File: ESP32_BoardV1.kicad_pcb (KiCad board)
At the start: 2 copper layers, 95 x 55 mm, 31 parts, among them J1 Jack-DC, J2 MODBUS RTU, J3 ISP, J4 EXT. IO 1, J5 To Sensor, J6 EXT. IO 1, Q1 UMH3N, U1 MAX485E, U2 ESP32-WROOM-32E(8MB), U3 RT9078-33GJ5

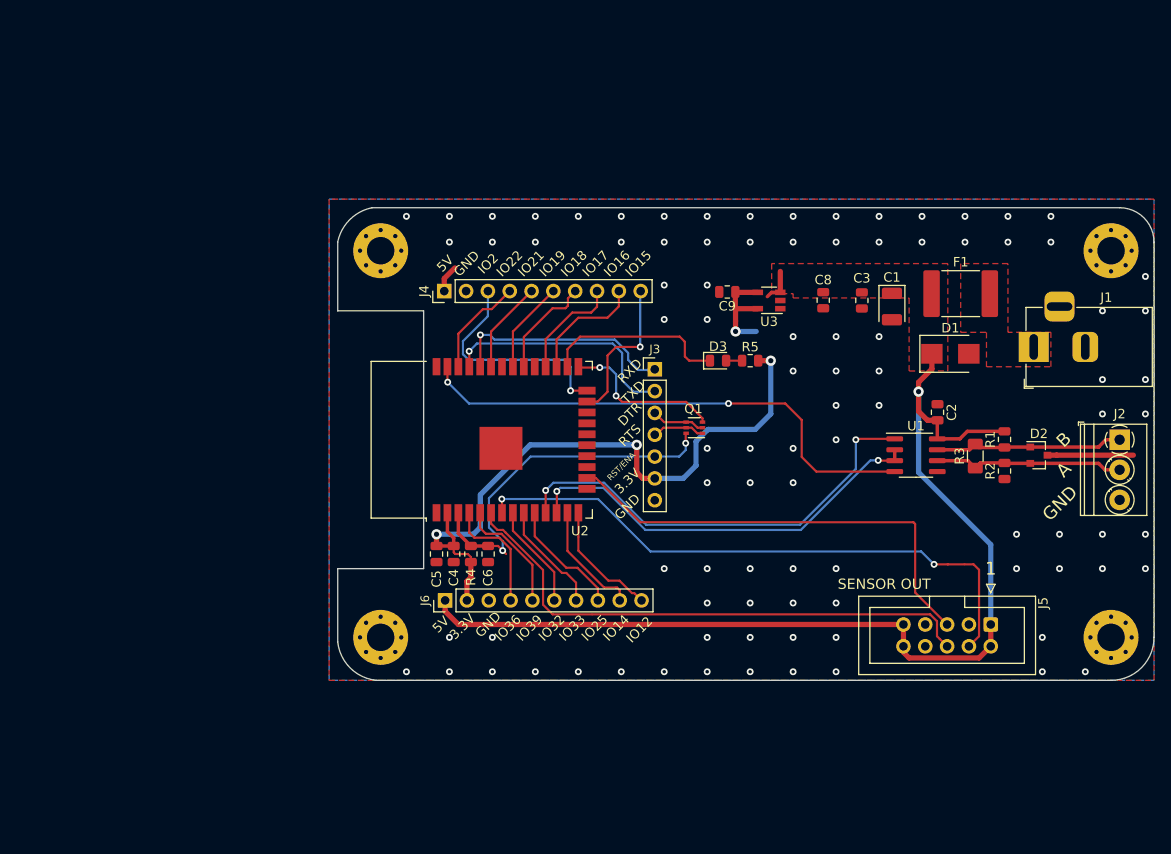
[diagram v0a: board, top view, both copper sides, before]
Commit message: Recreated PCB file
Removed old PCB files, Schematic error in existing PCB has been rectfied
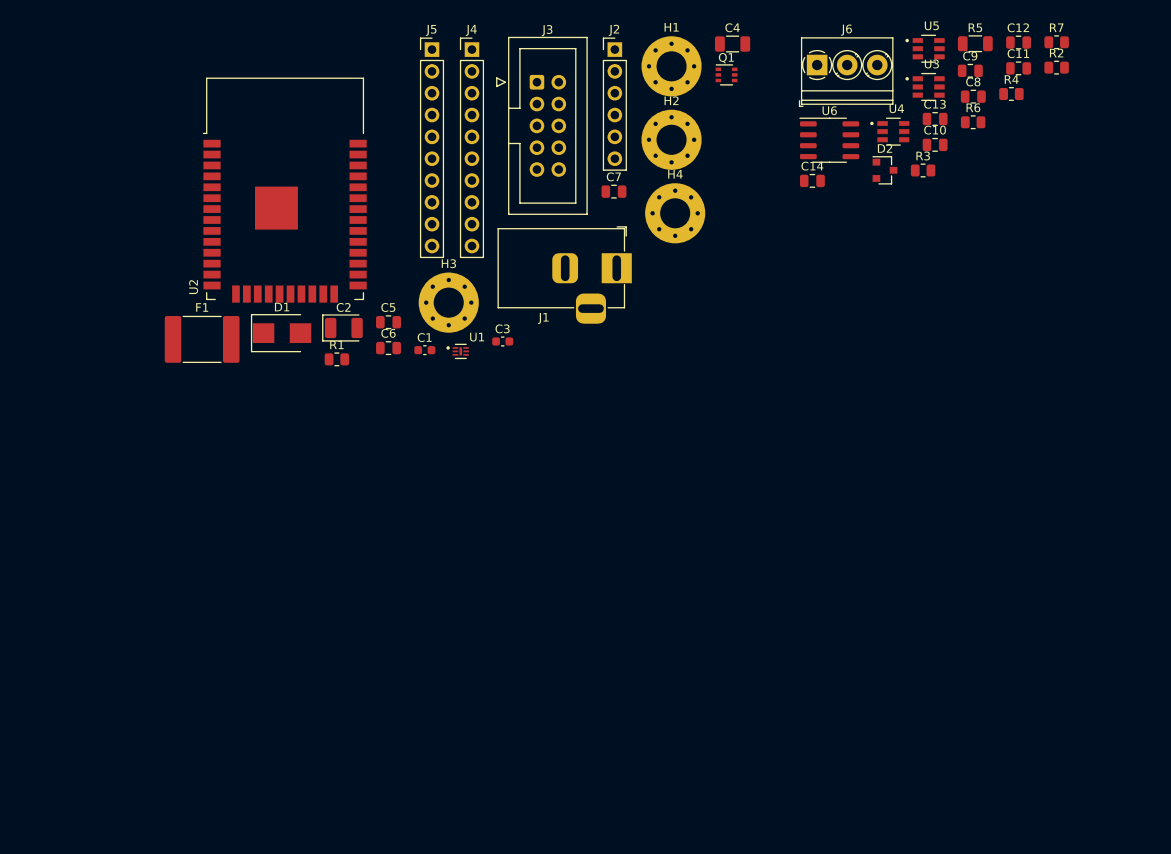
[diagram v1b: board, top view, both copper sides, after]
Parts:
- removed D3: LED, LED_SMD:LED_0805_2012Metric
- added C10: 10uF, Capacitor_SMD:C_0805_2012Metric, F.Cu at (191.5, 77.7)
- added C11: 10uF, Capacitor_SMD:C_0805_2012Metric, F.Cu at (201.2, 68.8)
- added C12: 10uF, Capacitor_SMD:C_0805_2012Metric, F.Cu at (201.2, 65.8)
- added C13: 10uF, Capacitor_SMD:C_0805_2012Metric, F.Cu at (191.5, 74.7)
- added C14: 0.1uF, Capacitor_SMD:C_0805_2012Metric, F.Cu at (177.2, 81.9)
- added C7: 0.1uF, Capacitor_SMD:C_0805_2012Metric, F.Cu at (154.2, 83.1)
- added R6: 10k, Resistor_SMD:R_0805_2012Metric, F.Cu at (196.0, 75.1)
- added R7: 10k, Resistor_SMD:R_0805_2012Metric, F.Cu at (205.7, 65.7)
- added U4: TXB0101DBVR, SnapEDA Library:SOT95P280X145-6N, F.Cu at (186.7, 76.1)
- added U5: TXB0101DBVR, SnapEDA Library:SOT95P280X145-6N, F.Cu at (190.8, 66.5)
- added U6: MAX485E, Package_SO:SOIC-8_3.9x4.9mm_P1.27mm, F.Cu at (179.2, 77.1)
- C1: value 100uF -> 2.2uF; footprint Capacitor_Tantalum_SMD:CP_EIA-3528-21_Kemet-B -> Capacitor_SMD:C_0603_1608Metric
- C2: value 0.1uF -> 100uF; footprint Capacitor_SMD:C_0805_2012Metric -> Capacitor_Tantalum_SMD:CP_EIA-3528-21_Kemet-B
- C3: value 0.1uF -> 2.2uF; footprint Capacitor_SMD:C_0805_2012Metric -> Capacitor_SMD:C_0603_1608Metric
- C4: value 10uF -> 100uF; footprint Capacitor_SMD:C_0805_2012Metric -> Capacitor_SMD:C_1206_3216Metric
- C5: value 0.1uF -> 10uF
- C8, C9: value 2.2uF -> 10uF
- H1, H2, H3, H4: value MountingHole -> MountingHole_Pad; footprint MountingHole:MountingHole_3.2mm_M3_Pad_Via -> MountingHole:MountingHole_3.5mm_Pad_Via
- J1: value Jack-DC -> Barrel_Jack_Switch
- J2: value MODBUS RTU -> ISP; footprint TerminalBlock_Phoenix:TerminalBlock_Phoenix_PT-1,5-3-3.5-H_1x03_P3.50mm_Horizontal -> Connector_PinHeader_2.54mm:PinHeader_1x06_P2.54mm_Vertical
- J3: value ISP -> To Sensor; footprint Connector_PinHeader_2.54mm:PinHeader_1x07_P2.54mm_Vertical -> Connector_IDC:IDC-Header_2x05_P2.54mm_Vertical
- J5: value To Sensor -> EXT. IO 1; footprint Connector_IDC:IDC-Header_2x05_P2.54mm_Vertical -> Connector_PinHeader_2.54mm:PinHeader_1x10_P2.54mm_Vertical
- J6: value EXT. IO 1 -> MODBUS RTU; footprint Connector_PinHeader_2.54mm:PinHeader_1x10_P2.54mm_Vertical -> TerminalBlock_Phoenix:TerminalBlock_Phoenix_PT-1,5-3-3.5-H_1x03_P3.50mm_Horizontal
- R1: value 4K7 -> 10K
- R2: value 4K7 -> 10k
- R3: value 120R -> 10k; footprint Resistor_SMD:R_1206_3216Metric -> Resistor_SMD:R_0805_2012Metric
- R4: value 10K -> 10k
- R5: value 1K -> 120R; footprint Resistor_SMD:R_0805_2012Metric -> Resistor_SMD:R_1206_3216Metric
- U1: value MAX485E -> MIC5528-3.3YMT-TR; footprint Package_SO:SOIC-8_3.9x4.9mm_P1.27mm -> SnapEDA Library:SON40P120X120X60-7N
- U3: value RT9078-33GJ5 -> TXB0101DBVR; footprint Package_TO_SOT_SMD:TSOT-23-5 -> SnapEDA Library:SOT95P280X145-6N
- moved J5 93.3 mm to (133.0, 66.6), turned to 0 degrees
- moved F1 88.4 mm to (106.2, 100.3)
- moved R4 82.6 mm to (200.4, 71.8), turned to 0 degrees
- moved R1 78.3 mm to (121.9, 102.6), turned to 0 degrees
- moved D1 77.8 mm to (115.5, 99.6)
- moved J6 75.9 mm to (177.8, 68.4), turned to 0 degrees
- moved J2 74.2 mm to (154.3, 66.6), turned to 0 degrees
- moved H4 70.8 mm to (161.3, 85.6)
- moved C2 69.8 mm to (122.7, 99.0), turned to 0 degrees
- moved C4 67.6 mm to (168.0, 65.9), turned to 0 degrees
- moved C1 54.6 mm to (132.1, 101.6), turned to 0 degrees
- moved U1 54.3 mm to (136.3, 101.7)
- moved H2 52.7 mm to (160.9, 77.1)
- moved J1 49.4 mm to (154.5, 92.0), turned to 0 degrees
- moved R2 47.3 mm to (205.7, 68.7), turned to 0 degrees
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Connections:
- C1 pad 2: GND -> +5V
- C2 pad 1: GND -> +5V
- C3 pad 1: +5V -> +3V3
- C3 pad 2: GND -> +5V
- C4 pad 1: +3V3 -> /RESET
- C4 pad 2: GND -> +5V
- C5 pad 2: GND -> +5V
- C6 pad 2: GND -> +5V
- C8 pad 1: +5V -> +3V3
- C8 pad 2: GND -> +5V
- C9 pad 2: GND -> +5V
- D1 pad 2: GND -> +5V
- D2 pad 1: /B -> /Modubus/B
- D2 pad 2: /A -> /Modubus/A
- D2 pad 3: GND -> +5V
- H1 pad 1: (no net) -> +5V
- H2 pad 1: (no net) -> +5V
- H3 pad 1: (no net) -> +5V
- H4 pad 1: (no net) -> +5V
- J1 pad 2: GND -> +5V
- J1 pad 3: (no net) -> +5V
- J2 pad 1: /B -> /UART0_RXD
- J2 pad 2: /A -> /UART0_TXD
- J2 pad 3: GND -> /DTR
- J3 pad 1: /UART0_RXD -> +5V
- J3 pad 2: /UART0_TXD -> +5V
- J3 pad 3: /DTR -> +5V
- J3 pad 4: /RTS -> /GAS_AOUT
- J3 pad 5: /RESET -> /SHARP_ILED
- J3 pad 6: +3V3 -> /SHARP_AOUT
- J3 pad 7: GND -> Net-(J3-Pad7)
- J4 pad 2: GND -> +5V
- J5 pad 10: +5V -> /IO12
- J5 pad 2: +5V -> +3V3
- J5 pad 3: GND -> +5V
- J5 pad 4: /GAS_AOUT -> /IO36
- J5 pad 5: /SHARP_ILED -> /IO39
- J5 pad 6: /SHARP_AOUT -> /IO32
- J5 pad 7: (no net) -> /IO33
- J5 pad 8: GND -> /IO25
- J5 pad 9: +5V -> /IO14
- J6 pad 1: +5V -> /Modubus/B
- J6 pad 2: +3V3 -> /Modubus/A
- J6 pad 3: GND -> +5V
- R1 pad 1: /B -> +3V3
- R1 pad 2: +5V -> /RESET
- R2 pad 1: GND -> +5V
- R2 pad 2: /A -> /Modubus/MODBUS_TXD5V
- R3 pad 1: /A -> +5V
- R3 pad 2: /B -> /Modubus/MODBUS_RXD5V
- R4 pad 1: +3V3 -> +5V
- R4 pad 2: /RESET -> /Modubus/MODBUS_EN5V
- R5 pad 1: +3V3 -> /Modubus/A
- R5 pad 2: Net-(D3-Pad2) -> /Modubus/B
- U1 pad 1: /MODBUS_RXD -> +3V3
- U1 pad 2: /MODBUS_EN -> +3V3
- U1 pad 3: /MODBUS_EN -> +5V
- U1 pad 4: /MODBUS_TXD -> +5V
- U1 pad 5: GND -> (no net)
- U1 pad 6: /A -> +5V
- U1 pad 7: /B -> +5V
- U2 pad 1: GND -> +5V
- U2 pad 15: GND -> +5V
- U2 pad 17: (no net) -> Net-(U2-Pad17)
- U2 pad 18: (no net) -> Net-(U2-Pad18)
- U2 pad 19: (no net) -> Net-(U2-Pad19)
- U2 pad 20: (no net) -> Net-(U2-Pad20)
- U2 pad 21: (no net) -> Net-(U2-Pad21)
- U2 pad 22: (no net) -> Net-(U2-Pad22)
- U2 pad 26: Net-(D3-Pad1) -> /IO4
- U2 pad 29: (no net) -> /IO5
- U2 pad 32: (no net) -> Net-(U2-Pad32)
- U2 pad 38: GND -> +5V
- U2 pad 39: GND -> +5V
- U3 pad 1: +5V -> +3V3
- U3 pad 2: GND -> +5V
- U3 pad 3: +5V -> /Modubus/MODBUS_EN
- U3 pad 4: +3V3 -> /Modubus/MODBUS_EN5V
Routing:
- net +5V: track 130.5 -> 0.00 mm, vias 1 -> 0
- net +3V3: track 89.1 -> 0.00 mm, vias 4 -> 0
- net /GAS_AOUT: track 70.0 -> 0.00 mm, vias 2 -> 0
- net /SHARP_AOUT: track 63.6 -> 0.00 mm
- net /MODBUS_TXD: track 60.7 -> 0.00 mm, vias 2 -> 0
- net /SHARP_ILED: track 53.6 -> 0.00 mm
- net /MODBUS_RXD: track 51.8 -> 0.00 mm, vias 2 -> 0
- net /MODBUS_EN: track 48.7 -> 0.00 mm, vias 2 -> 0
- net /RESET: track 42.9 -> 0.00 mm, vias 2 -> 0
- net /UART0_TXD: track 28.1 -> 0.00 mm, vias 1 -> 0
- net /IO2: track 26.4 -> 0.00 mm, vias 1 -> 0
- net /UART0_RXD: track 26.3 -> 0.00 mm, vias 1 -> 0
- net /A: track 22.9 -> 0.00 mm
- net /B: track 22.5 -> 0.00 mm
- net Net-(D3-Pad1): track 21.4 -> 0.00 mm
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- removed copper zone on F.Cu, net +5V
- removed copper zone on B.Cu, net GND
- removed copper zone on F.Cu, net GND
- removed copper zone on F.Cu, net Net-(F1-Pad2)
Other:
- board outline removed
- board text removed: "1"
- board text removed: "3.3V"
- board text removed: "5V"
- board text removed: "A"
- board text removed: "B"
- board text removed: "DTR"
- board text removed: "GND"
- board text removed: "IO12"
- board text removed: "IO14"
- board text removed: "IO15"
- board text removed: "IO16"
- board text removed: "IO17"
- board text removed: "IO18"
- board text removed: "IO19"
- board text removed: "IO2"
- board text removed: "IO21"
- board text removed: "IO22"
- board text removed: "IO25"
- board text removed: "IO32"
- board text removed: "IO33"
- board text removed: "IO36"
- board text removed: "IO39"
- board text removed: "RST/ENA"
- board text removed: "RTS"
- board text removed: "RXD"
- board text removed: "SENSOR OUT"
- board text removed: "TXD"

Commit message: 24.12.21
Board layout added, Step file added
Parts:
- removed C11, C12, C13: 10uF, Capacitor_SMD:C_0805_2012Metric
- removed the C4 at (168.0, 65.9)
- removed the C8 at (196.0, 72.1)
- removed the R6 at (196.0, 75.1)
- removed U4, U5: TXB0101DBVR, SnapEDA Library:SOT95P280X145-6N
- removed U6: MAX485E, Package_SO:SOIC-8_3.9x4.9mm_P1.27mm
- added C7: 0.1uF, Capacitor_SMD:C_0402_1005Metric_Pad0.74x0.62mm_HandSolder, F.Cu at (105.0, 105.0)
- added J7: Display, Connector_FFC-FPC:Hirose_FH12-40S-0.5SH_1x40-1MP_P0.50mm_Horizontal, F.Cu at (180.0, 125.0)
- added JP1: SolderJumper_2_Open, Resistor_SMD:R_0402_1005Metric_Pad0.72x0.64mm_HandSolder, F.Cu at (116.5, 103.5)
- added JP2: SolderJumper_2_Open, Resistor_SMD:R_0402_1005Metric_Pad0.72x0.64mm_HandSolder, F.Cu at (116.5, 105.0)
- added R10: 10k, Resistor_SMD:R_0402_1005Metric_Pad0.72x0.64mm_HandSolder, F.Cu at (174.0, 116.5)
- added R2: 10k, Resistor_SMD:R_0402_1005Metric_Pad0.72x0.64mm_HandSolder, F.Cu at (105.0, 103.5)
- added R7: 10k, Resistor_SMD:R_0805_2012Metric, F.Cu at (134.0, 105.8)
- added R9: 10k, Resistor_SMD:R_0402_1005Metric_Pad0.72x0.64mm_HandSolder, F.Cu at (174.0, 114.0)
- added SW1: SW_SPDT, Button_Switch_THT:SW_Slide_1P2T_CK_OS102011MS2Q, F.Cu at (102.8, 98.0)
- C1: value 2.2uF -> 10uF; footprint Capacitor_SMD:C_0603_1608Metric -> Capacitor_SMD:CP_Elec_3x5.4
- C10: value 10uF -> 0.1uF; footprint Capacitor_SMD:C_0805_2012Metric -> Capacitor_SMD:C_0402_1005Metric_Pad0.74x0.62mm_HandSolder
- C3: value 2.2uF -> 22uF; footprint Capacitor_SMD:C_0603_1608Metric -> Capacitor_SMD:CP_Elec_5x5.4
- C9: footprint Capacitor_SMD:C_0805_2012Metric -> Capacitor_SMD:C_0402_1005Metric_Pad0.74x0.62mm_HandSolder
- J1: footprint Connector_BarrelJack:BarrelJack_Horizontal -> Connector_BarrelJack:BarrelJack_CLIFF_FC681465S_SMT_Horizontal
- J3: value To Sensor -> GPIO expanded; footprint Connector_IDC:IDC-Header_2x05_P2.54mm_Vertical -> SnapEDA Library:JST_SM04B-SRSS-TB(LF)(SN)
- J4: value EXT. IO 1 -> sensor; footprint Connector_PinHeader_2.54mm:PinHeader_1x10_P2.54mm_Vertical -> connector:JST_SM05B-SRSS-TB(LF)(SN)
- J5: value EXT. IO 1 -> I2C extended; footprint Connector_PinHeader_2.54mm:PinHeader_1x10_P2.54mm_Vertical -> SnapEDA Library:JST_SM04B-SRSS-TB(LF)(SN)
- J6: footprint TerminalBlock_Phoenix:TerminalBlock_Phoenix_PT-1,5-3-3.5-H_1x03_P3.50mm_Horizontal -> SnapEDA Library:JST_SM03B-SRSS-TB(LF)(SN)
- R3: renamed from R2; value 10k -> 10K
- R4: renamed from R3; value 10k -> 10K
- R5: renamed from R4; value 10k -> 10K
- U1: value MIC5528-3.3YMT-TR -> AZ1117-3.3; footprint SnapEDA Library:SON40P120X120X60-7N -> Package_TO_SOT_SMD:SOT-223-3_TabPin2
- U3: value TXB0101DBVR -> MAX3485; footprint SnapEDA Library:SOT95P280X145-6N -> Package_SO:SOIC-8_3.9x4.9mm_P1.27mm
- moved H2 103.1 mm to (89.0, 151.0)
- moved R3 89.0 mm to (133.2, 120.5), turned to 90 degrees
- moved H3 85.9 mm to (201.0, 151.0)
- moved R5 84.6 mm to (131.2, 120.5), turned to 90 degrees
- moved C6 81.5 mm to (93.0, 137.0), turned to 180 degrees
- moved H1 78.0 mm to (89.0, 99.0)
- moved R8 75.2 mm to (142.0, 105.8)
- moved Q1 73.4 mm to (121.0, 126.5), turned to 180 degrees
- moved R6 70.5 mm to (138.0, 105.8)
- moved C9 70.1 mm to (176.5, 136.5), turned to 270 degrees
- moved U3 70.0 mm to (138.5, 117.5)
- moved R4 66.2 mm to (133.2, 114.5), turned to 270 degrees
- moved J2 66.0 mm to (114.0, 118.9)
- moved C10 61.1 mm to (175.0, 136.5), turned to 270 degrees
- moved J1 59.5 mm to (141.0, 150.0), turned to 90 degrees
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- renumbered C5 to C4, C6 to C5, C7 to C6, C14 to C8, R5 to R6, R7 to R8
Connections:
- C1 pad 2: +5V -> GND
- C10 pad 2: +5V -> GND
- C2 pad 2: +5V -> GND
- C3 pad 2: +5V -> GND
- C4 pad 2: +5V -> GND
- C5 pad 2: +5V -> GND
- C6 pad 2: +5V -> GND
- C8 pad 1: +5V -> GND
- C8 pad 2: +5V -> +3V3
- C9 pad 2: +5V -> GND
- D1 pad 2: +5V -> GND
- D2 pad 3: +5V -> GND
- H1 pad 1: +5V -> GND
- H2 pad 1: +5V -> GND
- H3 pad 1: +5V -> GND
- H4 pad 1: +5V -> GND
- J1 pad 2: +5V -> GND
- J1 pad 3: +5V -> GND
- J2 pad 6: +5V -> GND
- J3 pad 1: +5V -> /GPIO15
- J3 pad 2: +5V -> /GPIO16
- J3 pad 3: +5V -> /GPIO33
- J3 pad 4: /GAS_AOUT -> /GPIO32
- J4 pad 2: +5V -> /GAS_AOUT
- J4 pad 3: /IO2 -> /SHARP_AOUT
- J4 pad 4: /IO22 -> /SHARP_ILED
- J4 pad 5: /IO21 -> GND
- J5 pad 1: +5V -> /VCC
- J5 pad 2: +3V3 -> CTP_SCL
- J5 pad 3: +5V -> CTP_SDA
- J5 pad 4: /IO36 -> GND
- J6 pad 3: +5V -> GND
- R3 pad 1: +5V -> +3V3
- R3 pad 2: /Modubus/MODBUS_TXD5V -> /Modubus/MODBUS_TXD
- R4 pad 1: +5V -> +3V3
- R4 pad 2: /Modubus/MODBUS_RXD5V -> /Modubus/MODBUS_RXD
- R5 pad 1: +5V -> +3V3
- R5 pad 2: /Modubus/MODBUS_EN5V -> /Modubus/MODBUS_EN
- R8 pad 2: +5V -> +3V3
- U1 pad 1: +3V3 -> GND
- U2 pad 1: +5V -> GND
- U2 pad 10: /IO25 -> CTP_INT
- U2 pad 13: /IO14 -> TFT_RST
- U2 pad 14: /IO12 -> Net-(U2-Pad14)
- U2 pad 15: +5V -> GND
- U2 pad 23: /IO15 -> /GPIO15
- U2 pad 24: /IO2 -> Net-(U2-Pad24)
- U2 pad 26: /IO4 -> TFT_AO
- U2 pad 27: /IO16 -> Net-(SW1-Pad2)
- U2 pad 28: /IO17 -> /GPIO17
- U2 pad 29: /IO5 -> TFT_CS
- U2 pad 30: /IO18 -> TFT_SCLK
- U2 pad 31: /IO19 -> TFT_SDI
- U2 pad 33: /IO21 -> CTP_SDA
- U2 pad 36: /IO22 -> CTP_SCL
- U2 pad 38: +5V -> GND
- U2 pad 39: +5V -> GND
- U2 pad 8: /IO32 -> /GPIO32
- U2 pad 9: /IO33 -> /GPIO33
- U3 pad 1: +3V3 -> /Modubus/MODBUS_RXD
- U3 pad 2: +5V -> /Modubus/MODBUS_EN
- U3 pad 4: /Modubus/MODBUS_EN5V -> /Modubus/MODBUS_TXD
- U3 pad 5: +3V3 -> GND
- U3 pad 6: +5V -> /Modubus/A
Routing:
- net /DTR: track 0.00 -> 8.99 mm
- net /RTS: track 0.00 -> 8.24 mm
- net /RESET: track 0.00 -> 6.85 mm
- net GND: vias 0 -> 37
- added copper zone on F.Cu, net +3V3
- added copper zone on F.Cu, net +5V
- added copper zone on B.Cu, net GND
- added copper zone on F.Cu, net Net-(F1-Pad2)
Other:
- board outline added: 120 x 60 mm
- board text added: "DTR"
- board text added: "GND"
- board text added: "RST"
- board text added: "RTS"
- board text added: "RXD"
- board text added: "TXD"

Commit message: PCB completed
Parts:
- moved J4 63.5 mm to (100.5, 153.0), turned to 0 degrees
- moved J5 49.6 mm to (124.4, 149.0), turned to 0 degrees
- moved J3 49.3 mm to (112.7, 149.0), turned to 0 degrees
- moved J6 48.5 mm to (135.6, 149.0), turned to 0 degrees
- moved JP1 43.8 mm to (122.0, 147.0), turned to 0 degrees
- moved JP2 40.9 mm to (122.0, 145.5), turned to 0 degrees
- moved R7 39.1 mm to (131.5, 144.8)
- moved R6 39.1 mm to (135.6, 144.8)
- moved R8 39.1 mm to (139.8, 144.8)
- moved C3 23.1 mm to (181.0, 148.8), turned to 90 degrees
- moved D1 15.3 mm to (165.0, 137.0), turned to 90 degrees
- moved D2 13.6 mm to (135.6, 128.2), turned to 270 degrees
- moved U1 12.6 mm to (173.5, 149.2)
- moved J1 12.0 mm to (153.0, 149.5)
- moved F1 12.0 mm to (153.0, 139.2)
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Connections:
- J3 pad 1: /GPIO15 -> /GPIO33
- J3 pad 2: /GPIO16 -> /GPIO17
- J3 pad 3: /GPIO33 -> /GPIO15
- J3 pad 4: /GPIO32 -> /GPIO16
- J4 pad 2: /GAS_AOUT -> /SHARP_AOUT
- J4 pad 3: /SHARP_AOUT -> /GAS_AOUT
- J6 pad 1: /Modubus/B -> /Modubus/A
- J6 pad 2: /Modubus/A -> GND
- J6 pad 3: GND -> /Modubus/B
- R3 pad 2: /Modubus/MODBUS_TXD -> MODBUS_TXD
- R4 pad 2: /Modubus/MODBUS_RXD -> MODBUS_RXD
- R5 pad 2: /Modubus/MODBUS_EN -> MODBUS_EN
- R7 pad 1: GND -> +3V3
- R8 pad 2: +3V3 -> GND
- U2 pad 10: CTP_INT -> /GPIO17
- U2 pad 11: /MODBUS_RXD -> MODBUS_RXD
- U2 pad 12: /MODBUS_EN -> MODBUS_EN
- U2 pad 16: /SHARP_ILED -> /GPIO16
- U2 pad 28: /GPIO17 -> CTP_INT
- U2 pad 37: /MODBUS_TXD -> MODBUS_TXD
- U2 pad 8: /GPIO32 -> /SHARP_ILED
- U3 pad 1: /Modubus/MODBUS_RXD -> MODBUS_RXD
- U3 pad 2: /Modubus/MODBUS_EN -> MODBUS_EN
- U3 pad 3: /Modubus/MODBUS_EN -> MODBUS_EN
- U3 pad 4: /Modubus/MODBUS_TXD -> MODBUS_TXD
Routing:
- net CTP_SDA: track 0.00 -> 139.1 mm, vias 0 -> 4
- net CTP_SCL: track 0.00 -> 138.3 mm, vias 0 -> 4
- net TFT_SDI: track 0.00 -> 93.3 mm
- net TFT_SCLK: track 0.00 -> 89.7 mm
- net +5V: track 0.00 -> 89.6 mm, vias 0 -> 1
- net TFT_CS: track 0.00 -> 86.5 mm
- net TFT_AO: track 0.00 -> 71.3 mm
- net TFT_RST: track 0.00 -> 70.9 mm, vias 0 -> 2
- net MODBUS_EN: track 0.00 -> 54.7 mm
- net MODBUS_RXD: track 0.00 -> 51.1 mm
- net MODBUS_TXD: track 0.00 -> 45.5 mm, vias 0 -> 2
- net +3V3: track 0.00 -> 41.7 mm, vias 0 -> 3
- net GND: track 0.00 -> 37.4 mm, vias 37 -> 56
- net /GPIO15: track 0.00 -> 34.4 mm, vias 0 -> 2
- net /RESET: track 6.85 -> 38.2 mm, vias 0 -> 1
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
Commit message: Schematics change
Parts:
- removed JP2: SolderJumper_2_Open, Resistor_SMD:R_0402_1005Metric_Pad0.72x0.64mm_HandSolder
- added REF**: WEEE-Logo_8.4x12mm_SilkScreen, Symbol:WEEE-Logo_8.4x12mm_SilkScreen, F.Cu at (167.5, 102.0)
- F1: footprint Fuse:Fuse_2920_7451Metric -> Fuse:Fuse_1206_3216Metric
- moved C7 6.75 mm to (111.8, 105.2)
- moved R2 6.75 mm to (111.8, 103.8)
- moved SW1 6.75 mm to (109.5, 97.8)
- moved JP1 2.83 mm to (120.0, 149.0), turned to 90 degrees
- moved F1 2.10 mm to (152.0, 141.0)
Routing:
- net CTP_INT: track 0.00 -> 86.3 mm
- net GND: track 37.4 -> 105.4 mm, vias 56 -> 72
- net +5V: track 89.6 -> 69.2 mm, vias 1 -> 3
- net TFT_SDI: track 93.3 -> 101.0 mm
- net TFT_SCLK: track 89.7 -> 96.2 mm
- net CTP_SCL: track 138.3 -> 144.5 mm
- net +3V3: track 41.7 -> 47.1 mm, vias 3 -> 2
- net TFT_CS: track 86.5 -> 91.4 mm
- net Net-(SW1-Pad2): track 22.4 -> 19.3 mm
- net CTP_SDA: track 139.1 -> 142.1 mm
- net /RESET: track 38.2 -> 40.9 mm
- net /UART0_RXD: track 18.7 -> 21.4 mm
- net MODBUS_TXD: track 45.5 -> 42.9 mm
- net /UART0_TXD: track 20.3 -> 22.4 mm
- net MODBUS_EN: track 54.7 -> 53.5 mm
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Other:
- outline, holes or cut-outs redrawn
- board text added: "A"
- board text added: "B"
- board text added: "GAS_AOUT"
- board text added: "GPI033"
- board text added: "GPIO15"
- board text added: "GPIO16"
- board text added: "GPIO17"
- board text added: "SCL"
- board text added: "SDA"
- board text added: "SEN_PWR"
- board text added: "SHARP_AOUT"
- board text added: "SHARP_ILED"
- board text added: "VCC"

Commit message: Final draft
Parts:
- removed JP1: SolderJumper_2_Open, Resistor_SMD:R_0402_1005Metric_Pad0.72x0.64mm_HandSolder
- removed REF**: WEEE-Logo_8.4x12mm_SilkScreen, Symbol:WEEE-Logo_8.4x12mm_SilkScreen
- added Q2: SS8050-G, Package_TO_SOT_SMD:SOT-23, F.Cu at (157.6, 133.4)
- added R11: 10K, Resistor_SMD:R_0402_1005Metric_Pad0.72x0.64mm_HandSolder, F.Cu at (154.8, 133.8)
- added R12: 10K, Resistor_SMD:R_0402_1005Metric_Pad0.72x0.64mm_HandSolder, F.Cu at (154.8, 134.8)
- added R13: 10R, Resistor_SMD:R_0402_1005Metric_Pad0.72x0.64mm_HandSolder, F.Cu at (171.2, 133.6)
- R7, R8: value 10k -> 5k
- moved R6 2.25 mm to (135.6, 142.5)
- moved R7 2.25 mm to (131.5, 142.5)
- moved R8 2.25 mm to (139.8, 142.5)
- moved C10 2.02 mm to (171.2, 134.6), turned to 180 degrees
- moved C7 1.85 mm to (111.8, 103.4)
- moved R2 1.35 mm to (111.8, 102.4)
- moved C9 1.20 mm to (171.2, 135.6), turned to 180 degrees
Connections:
- J3 pad 4: /GPIO16 -> +3V3
- J5 pad 1: /VCC -> +3V3
- J7 pad 2: GND -> /LED_K
- U2 pad 14: Net-(U2-Pad14) -> unconnected-(U2-Pad14)
- U2 pad 16: /GPIO16 -> /BL_CONTRL
- U2 pad 17: Net-(U2-Pad17) -> unconnected-(U2-Pad17)
- U2 pad 18: Net-(U2-Pad18) -> unconnected-(U2-Pad18)
- U2 pad 19: Net-(U2-Pad19) -> unconnected-(U2-Pad19)
- U2 pad 20: Net-(U2-Pad20) -> unconnected-(U2-Pad20)
- U2 pad 21: Net-(U2-Pad21) -> unconnected-(U2-Pad21)
- U2 pad 22: Net-(U2-Pad22) -> unconnected-(U2-Pad22)
- U2 pad 24: Net-(U2-Pad24) -> unconnected-(U2-Pad24)
- U2 pad 32: Net-(U2-Pad32) -> unconnected-(U2-Pad32)
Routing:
- net /BL_CONTRL: track 0.00 -> 50.3 mm, vias 0 -> 2
- net /GPIO16: track 24.6 -> 0.00 mm, vias 2 -> 0
- net GND: track 105.4 -> 82.6 mm, vias 72 -> 56
- net Net-(Q2-Pad3): track 0.00 -> 17.8 mm
- net MODBUS_TXD: track 42.9 -> 57.2 mm
- net +3V3: track 47.1 -> 37.0 mm, vias 2 -> 3
- net /VCC: track 4.78 -> 0.00 mm
- net Net-(Q2-Pad1): track 0.00 -> 2.20 mm
- net /LED_K: track 0.00 -> 2.16 mm
- net Net-(C7-Pad2): track 8.38 -> 6.36 mm, vias 1 -> 0
- net /UART0_RXD: track 21.4 -> 19.8 mm
- net /UART0_TXD: track 22.4 -> 21.1 mm
- net /SHARP_AOUT: track 17.0 -> 15.8 mm
- net /SHARP_ILED: track 16.9 -> 15.7 mm
- net /GPIO17: track 19.6 -> 18.8 mm
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- added copper zone on F.Cu, net GND
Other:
- net class Default removed
- board text added: "FAN"
- board text added: "GPIO"
- board text added: "I2C"
- board text added: "SENSOR"
- board text added: "Version 1.0"
- board text removed: "GPIO16"
